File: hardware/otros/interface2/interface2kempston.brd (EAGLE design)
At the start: 73.6 x 32.1 mm, 15 parts, among them IC1 74LS32N, IC2 74LS366N

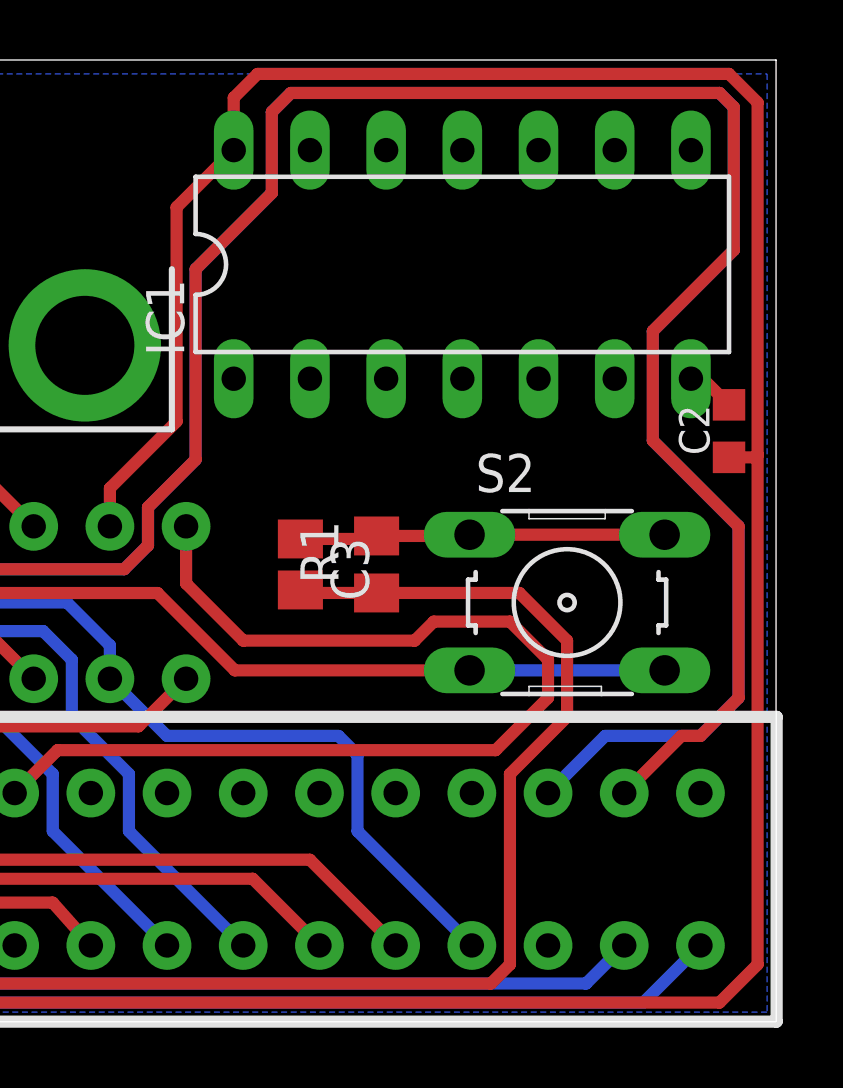
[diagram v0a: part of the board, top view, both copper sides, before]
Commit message: 
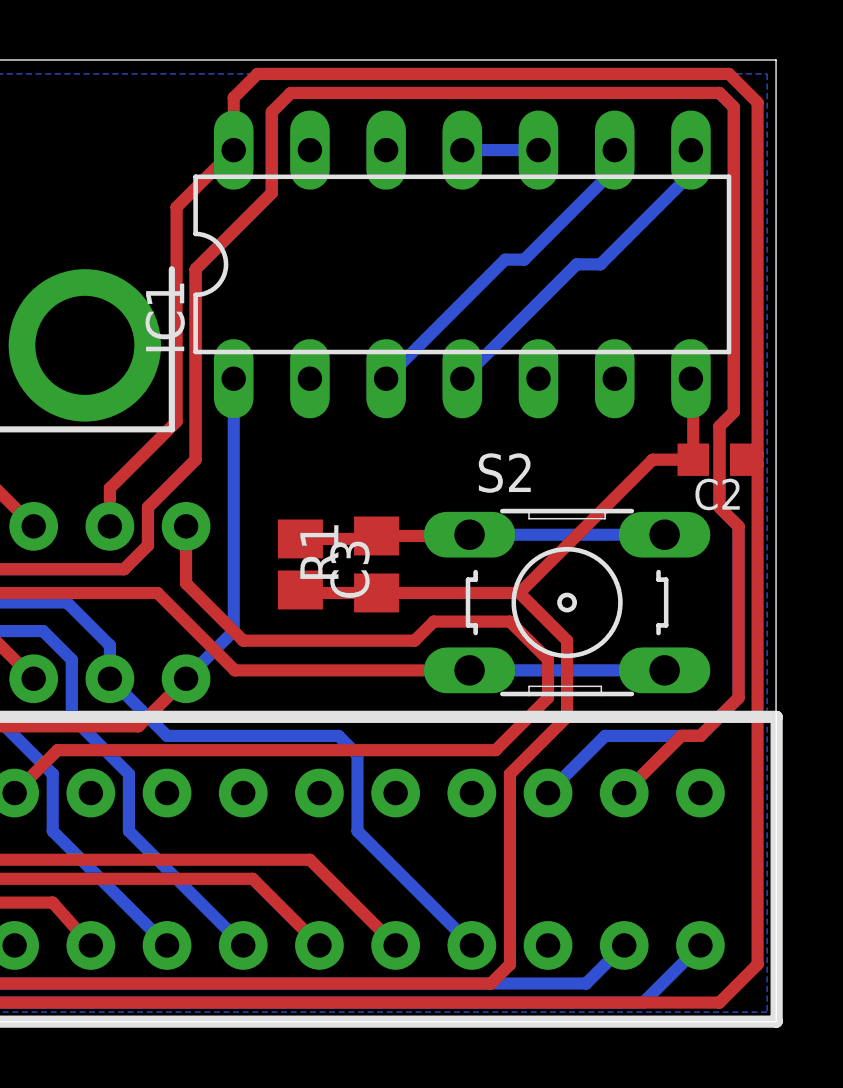
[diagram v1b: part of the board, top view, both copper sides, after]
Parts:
- moved C2 1.00 mm to (71.8, 18.7), turned to 180 degrees
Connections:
- net /RDIO: now also IC1.3; no longer IC1.6
- net A5: now also IC1.5; no longer IC1.2
- net D5: now also IC1.6; no longer IC1.3
- net IORQ: now also IC1.2; no longer IC1.5
- net KEMPSTON: now also IC1.4; no longer IC1.1
- net RD: now also IC1.1; no longer IC1.4
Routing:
- net KEMPSTON: track 0.00 -> 11.2 mm
- net /RDIO: track 0.00 -> 11.1 mm
- net RD: track 10.6 -> 21.2 mm
- net GND: track 116.9 -> 125.6 mm
- net N$4: track 0.00 -> 2.54 mm
- net A8: track 71.5 -> 69.6 mm
- net A10: track 81.6 -> 79.8 mm
